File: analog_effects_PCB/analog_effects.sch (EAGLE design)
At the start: 24 parts, among them J1 575-4, J2 575-4, U1 TL082

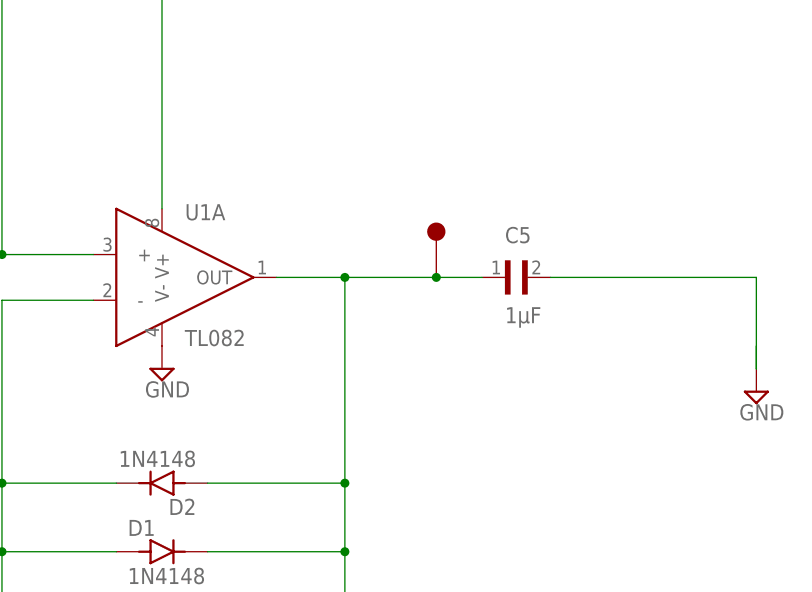
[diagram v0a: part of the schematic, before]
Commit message: added mux and digital pots to schematic
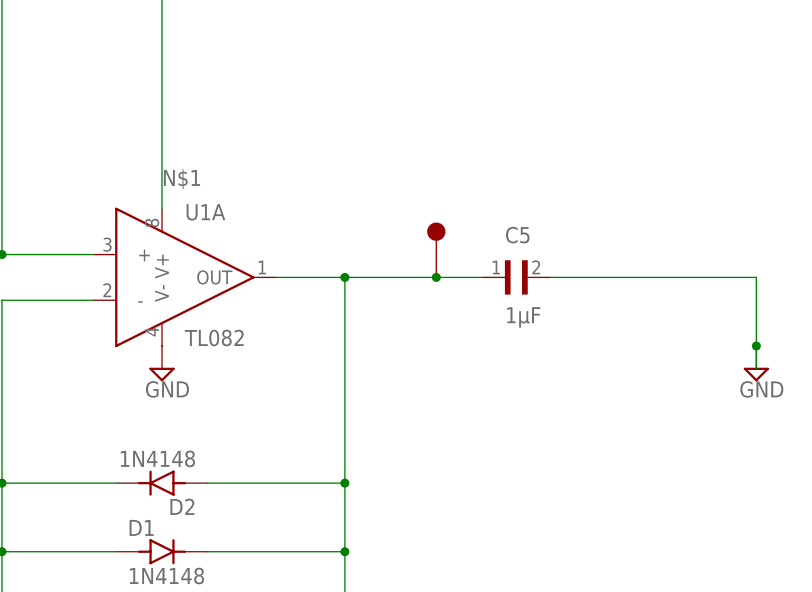
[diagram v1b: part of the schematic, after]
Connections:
- removed net N$10: C5.2
- net GND: now also C5.2
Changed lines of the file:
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@@
 <setting verticaltext="up"/>
 </settings>
-<grid distance="0.1" unitdist="inch" unit="inch" style="lines" multiple="1" display="no" altdistance="0.01" altunitdist="inch" altunit="inch"/>
+<grid distance="100" unitdist="mil" unit="mil" style="lines" multiple="1" display="no" altdistance="0.01" altunitdist="inch" altunit="inch"/>
 <layers>
 <layer number="1" name="Top" color="4" fill="1" visible="no" active="no"/>
@@
 <attribute name="VALUE" x="-17.78" y="116.8379" size="1.27105" layer="96"/>
 </instance>
-<instance part="SUPPLY4" gate="GND" x="182.88" y="99.06" smashed="yes">
-<attribute name="VALUE" x="180.975" y="95.885" size="1.778" layer="96"/>
+<instance part="SUPPLY4" gate="GND" x="182.88" y="101.6" smashed="yes">
+<attribute name="VALUE" x="180.975" y="98.425" size="1.778" layer="96"/>
 </instance>
 </instances>
@@
 <pinref part="R4" gate="G$1" pin="2"/>
 <wire x1="25.4" y1="180.34" x2="43.18" y2="180.34" width="0.1524" layer="91"/>
-<pinref part="U1" gate="A" pin="V+"/>
 <wire x1="43.18" y1="180.34" x2="106.68" y2="180.34" width="0.1524" layer="91"/>
-<wire x1="106.68" y1="180.34" x2="116.84" y2="180.34" width="0.1524" layer="91"/>
-<wire x1="116.84" y1="180.34" x2="116.84" y2="119.38" width="0.1524" layer="91"/>
 <junction x="43.18" y="180.34"/>
 <pinref part="TP5" gate="G$1" pin="TP"/>
-<junction x="106.68" y="180.34"/>
 <pinref part="BT1" gate="G$1" pin="+"/>
 <wire x1="0" y1="162.56" x2="0" y2="180.34" width="0.1524" layer="91"/>
 <wire x1="0" y1="180.34" x2="25.4" y2="180.34" width="0.1524" layer="91"/>
 <junction x="25.4" y="180.34"/>
+<pinref part="U1" gate="A" pin="V+"/>
+<wire x1="106.68" y1="180.34" x2="116.84" y2="180.34" width="0.1524" layer="91"/>
+<wire x1="116.84" y1="180.34" x2="116.84" y2="119.38" width="0.1524" layer="91"/>
+<junction x="106.68" y="180.34"/>
+<label x="116.84" y="121.92" size="1.778" layer="95"/>
 </segment>
 </net>
@@
 </segment>
 <segment>
+<pinref part="C5" gate="G$1" pin="2"/>
+<wire x1="160.02" y1="111.76" x2="182.88" y2="111.76" width="0.1524" layer="91"/>
+<wire x1="182.88" y1="111.76" x2="182.88" y2="104.14" width="0.1524" layer="91"/>
 <pinref part="SUPPLY4" gate="GND" pin="GND"/>
 <wire x1="182.88" y1="104.14" x2="182.88" y2="101.6" width="0.1524" layer="91"/>
+<junction x="182.88" y="104.14"/>
 </segment>
 </net>
@@
 <wire x1="91.44" y1="157.48" x2="93.98" y2="157.48" width="0.1524" layer="91"/>
 <pinref part="C3" gate="G$1" pin="2"/>
-<pinref part="U1" gate="A" pin="+"/>
 <wire x1="93.98" y1="157.48" x2="99.06" y2="157.48" width="0.1524" layer="91"/>
 <wire x1="71.12" y1="114.3" x2="83.82" y2="114.3" width="0.1524" layer="91"/>
 <wire x1="83.82" y1="114.3" x2="99.06" y2="114.3" width="0.1524" layer="91"/>
-<wire x1="99.06" y1="114.3" x2="109.22" y2="114.3" width="0.1524" layer="91"/>
 <wire x1="99.06" y1="157.48" x2="99.06" y2="114.3" width="0.1524" layer="91"/>
-<junction x="99.06" y="114.3"/>
 <pinref part="TP3" gate="G$1" pin="TP"/>
 <junction x="83.82" y="114.3"/>
 <pinref part="TP4" gate="G$1" pin="TP"/>
 <junction x="93.98" y="157.48"/>
+<pinref part="U1" gate="A" pin="+"/>
+<wire x1="99.06" y1="114.3" x2="109.22" y2="114.3" width="0.1524" layer="91"/>
+<junction x="99.06" y="114.3"/>
 </segment>
 </net>
@@
 </segment>
 </net>
-<net name="N$10" class="0">
-<segment>
-<pinref part="C5" gate="G$1" pin="2"/>
-<wire x1="160.02" y1="111.76" x2="182.88" y2="111.76" width="0.1524" layer="91"/>
-<wire x1="182.88" y1="111.76" x2="182.88" y2="101.6" width="0.1524" layer="91"/>
-</segment>
-</net>

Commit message: completed the digital pot circuitry on schematic
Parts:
- added J3: SAMTEC-SSQ-120-01-X-DJ, SAMTEC-SSQ-120-01-X-D:SAMTEC-SSQ-120-01-X-DJ
- added R10, R11, R12, R13, R14, R15, R7, R8, R9: 100kΩ, CRCW0603100KDHEAP:CRCW0603100KDHEAP
- added U2: AD5241BRZ1M, AD5241BRZ1M:AD5241BRZ1M
- added U3: AD5241BRZ10, AD5241BRZ10:AD5241BRZ10
- added U4: AD5241BRZ100, AD5241BRZ100:AD5241BRZ100
- added U5: TS5A3359DCUT, TS5A3359DCUT:TS5A3359DCUT
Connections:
- new net N$12: R10.1, U2.SHDN*
- new net N$13: R3.2, TP6.TP, U2.B1
- new net N$14: R11.2, U2.SDA
- new net N$15: R10.2, R11.1, R12.2, U2.VDD
- new net N$16: C5.2, U3.B1
- new net N$17: R12.1, U2.SCL
- new net N$19: R13.1, U4.SDA
- new net N$20: R13.2, R14.2, R15.2, U4.VDD
- new net N$21: R15.1, U4.SCL
- new net N$22: U3.W1, U4.B1
- new net N$23: R14.1, U4.~SHDN
- new net N$24: R7.1, U3.SDA
- new net N$25: R7.2, R8.2, R9.2, U3.VDD
- new net N$26: R9.1, U3.~SHDN
- new net N$27: R8.1, U3.SCL
- net GND: now also U2.AD0, U2.AD1, U2.DGND, U2.VSS, U3.AD0, U3.AD1, U3.DGND, U3.VSS, U4.AD0, U4.AD1, U4.DGND, U4.VSS, U4.W1; no longer C5.2
- net N$5: now also U2.W1; no longer R3.2, TP6.TP
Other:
- moved on the sheet: BT1, C1, C2, C3, C4, C5, C7, D1, D2, J1, J2, R1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

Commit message: Partly added Fuzz Circuit
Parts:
- added BT2: BC9VPC, BC9VPC:BC9VPC
- added C6: GRM188R6YA225KA12D, GRM188R6YA225KA12D:GRM188R6YA225KA12D
- added Q1, Q2: (no value), ngspice-simulation:BJT_PNP
- added R16: 100kΩ, CRCW0603100KDHEAP:CRCW0603100KDHEAP
- added R17: CRCW060333K0JNEAHP, CRCW060333K0JNEAHP:CRCW060333K0JNEAHP
- added R18: CRCW06038K20FKEAC, CRCW06038K20FKEAC:CRCW06038K20FKEAC
- added R19: CRCW0603470RJNEBC, CRCW0603470RJNEBC:CRCW0603470RJNEBC
- added U7: AD5258BRMZ1-R7, AD5258BRMZ1-R7:AD5258BRMZ1-R7
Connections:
- new net FUZZ_IN: C6.1
- new net N$10: Q1.E, Q2.B, R17.1
- new net N$11: BT2.-, R17.2, R19.2
- new net N$18: R18.1, R19.1
- new net N$28: Q2.C, R16.2
- new net N$9: C6.2, Q1.B, R16.1
- net GND: now also Q1.C
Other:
- moved on the sheet: BT1, C1, C2, C3, C4, C5, C7, D1, D2, J1, J2, J3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

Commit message: Added Mux logic to schematic. need to connect to Effects and decide if we have effect c or use as pass through
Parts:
- added C8: GCM188R91E104KA37J, GCM188R91E104KA37J:GCM188R91E104KA37J
- added C9: GRM188R61A226ME15D, GRM188R61A226ME15D:GRM188R61A226ME15D
- added U10, U11, U12, U13, U14, U8, U9: TS5A3359DCUT, TS5A3359DCUT:TS5A3359DCUT
- added U6: AD5258BRMZ1-R7, AD5258BRMZ1-R7:AD5258BRMZ1-R7
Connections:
- new net AUDIO_IN: U12.NO0, U13.NO0, U14.NO0
- new net A_OUT: U10.NO0, U11.NO0, U9.NO0
- new net B_OUT: U10.NO1, U11.NO1, U9.NO1
- new net C_OUT: U10.NO2, U11.NO2, U9.NO2
- new net MUX1_OUT: U10.COM, U12.NO1, U13.NO1, U14.NO1
- new net MUX1_S1: U10.IN1
- new net MUX1_S2: U10.IN2
- new net MUX2_OUT: U12.NO2, U13.NO2, U14.NO2, U9.COM
- new net MUX2_S1: U9.IN1
- new net MUX2_S2: U9.IN2
- new net MUX3_OUT: U11.COM
- new net MUX3_S1: U11.IN1
- new net MUX3_S2: U11.IN2
- new net MUX4_OUT: U12.COM
- new net MUX4_S1: U12.IN1
- new net MUX4_S2: U12.IN2
- new net MUX5_OUT: U13.COM
- new net MUX5_S1: U13.IN1
- new net MUX5_S2: U13.IN2
- new net MUX6_OUT: U14.COM
- new net MUX6_S1: U14.IN1
- new net MUX6_S2: U14.IN2
- new net N$29: C9.2, U7.W
- new net N$30: C8.2, U6.W
- new net N$31: U6.B
- new net N$38: U10.VCC
- new net N$39: U11.VCC
- new net N$40: U9.VCC
- new net N$41: U13.VCC
- new net N$42: U12.VCC
- new net N$56: U14.VCC
- net GND: now also C9.1, U10.GND, U11.GND, U12.GND, U13.GND, U14.GND, U6.A, U6.GND, U7.A, U7.GND, U9.GND
- net N$18: now also C8.1
- net N$28: now also U7.B

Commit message: Fixed Fuzz pot but need to change volume pot to 500k
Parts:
- removed U8: TS5A3359DCUT, TS5A3359DCUT:TS5A3359DCUT
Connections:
- removed net FUZZ_IN: C6.1
- new net 5V: J3.1, U7.VDD, U7.VLOGIC
- new net FUZZ_P1_SCL: U7.SCL
- new net FUZZ_P1_SDA: U7.SDA
- new net FUZZ_P2_SCL: U6.SCL
- new net FUZZ_P2_SDA: U6.SDA
- net MUX4_OUT: now also C6.1

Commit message: Schematic almost finalized missing aux in and out and possibly push buttons, starting layout
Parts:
- removed J1, J2: 575-4, 575-4:575-4
- removed R10: 100kΩ, CRCW0603100KDHEAP:CRCW0603100KDHEAP
- removed U3: AD5241BRZ10, AD5241BRZ10:AD5241BRZ10
- removed U5: TS5A3359DCUT, TS5A3359DCUT:TS5A3359DCUT
- removed U6: AD5258BRMZ1-R7, AD5258BRMZ1-R7:AD5258BRMZ1-R7
- added C10, C11, C12, C13, C14, C15, C16, C17, C18, C19, C20, C21: GCM188R91E104KA37J, GCM188R91E104KA37J:GCM188R91E104KA37J
- added TP10, TP11, TP12, TP13, TP14, TP15, TP16, TP17, TP18, TP19, TP20, TP7, TP8, TP9: 5015, 5015:5015
- added U8: AD5241BRZ1M, AD5241BRZ1M:AD5241BRZ1M
- R11, R12, R13, R14, R15, R7, R8, R9: value 100kΩ -> 10kΩ; device CRCW0603100KDHEAP:CRCW0603100KDHEAP -> MCT06030D1002BP100:MCT06030D1002BP100
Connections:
- removed net FUZZ_P1_SCL: U7.SCL
- removed net FUZZ_P1_SDA: U7.SDA
- removed net FUZZ_P2_SCL: U6.SCL
- removed net FUZZ_P2_SDA: U6.SDA
- removed net N$16: C5.2, U3.B1
- removed net N$24: R7.1, U3.SDA
- removed net N$25: R7.2, R8.2, R9.2, U3.VDD
- removed net N$26: R9.1, U3.~SHDN
- removed net N$27: R8.1, U3.SCL
- removed net N$31: U6.B
- removed net N$38: U10.VCC
- removed net N$39: U11.VCC
- removed net N$40: U9.VCC
- removed net N$41: U13.VCC
- removed net N$42: U12.VCC
- removed net N$56: U14.VCC
- new net POT_SCL: J3.5, R11.2, R12.2, R14.2, R7.2
- new net POT_SDA: J3.3, R13.1, R15.1, R8.1, R9.1
- net 5V: now also C10.2, C11.2, C12.2, C13.2, C14.2, C15.2, C16.2, C17.2, C18.2, C19.2, C20.2, C21.2, J3.2, TP19.TP, TP20.TP, U10.VCC, U11.VCC, U12.VCC, U13.VCC, U14.VCC, U2.SHDN*, U2.VDD, U4.AD1, U4.VDD, U4.~SHDN, U7.AD0, U7.AD1, U8.AD0, U8.SHDN*, U8.VDD, U9.VCC; no longer J3.1
- net A_OUT: now also TP12.TP, U8.B1
- net B_OUT: now also U4.W1
- net GND: now also C10.1, C11.1, C12.1, C13.1, C14.1, C15.1, C16.1, C17.1, C18.1, C19.1, C20.1, C21.1, J3.39, U8.AD1, U8.DGND, U8.VSS; no longer J2.1, U3.AD0, U3.AD1, U3.DGND, U3.VSS, U4.AD1, U4.W1, U6.A, U6.GND
- net MUX1_OUT: now also TP16.TP
- net MUX1_S1: now also J3.7
- net MUX1_S2: now also J3.29
- net MUX2_OUT: now also TP17.TP
- net MUX2_S1: now also J3.31
- net MUX2_S2: now also J3.26
- net MUX3_OUT: now also TP18.TP
- net MUX3_S1: now also J3.24
- net MUX3_S2: now also J3.21
- net MUX4_OUT: now also TP13.TP
- net MUX4_S1: now also J3.19
- net MUX4_S2: now also J3.23
- net MUX5_OUT: now also R1.1, TP14.TP
- net MUX5_S1: now also J3.32
- net MUX5_S2: now also J3.33
- net MUX6_OUT: now also TP15.TP
- net MUX6_S1: now also J3.8
- net MUX6_S2: now also J3.10
- net N$10: now also TP8.TP
- net N$11: now also TP9.TP
- net N$12: now also R8.2, U2.SDA; no longer R10.1, U2.SHDN*
- net N$14: now also R12.1, U8.SCL; no longer R11.2, U2.SDA
- net N$15: now also R9.2, U4.SDA; no longer R10.2, R11.1, R12.2, U2.VDD
- net N$17: now also R7.1; no longer R12.1
- net N$19: now also R13.2, U8.SDA; no longer R13.1, U4.SDA
- net N$20: now also R14.1, U7.SCL; no longer R13.2, R14.2, R15.2, U4.VDD
- net N$21: now also R11.1; no longer R15.1
- net N$22: now also C5.2; no longer U3.W1
- net N$23: now also R15.2, U7.SDA; no longer R14.1, U4.~SHDN
- net N$29: now also TP11.TP
- net N$30: now also TP10.TP, U8.A1; no longer U6.W
- net N$8: now also Q2.E, R18.2; no longer J1.1, R1.1
- net N$9: now also TP7.TP
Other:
- moved on the sheet: Q2, R11, R12, R13, R14, R15, R7, R8, R9, U2, U4

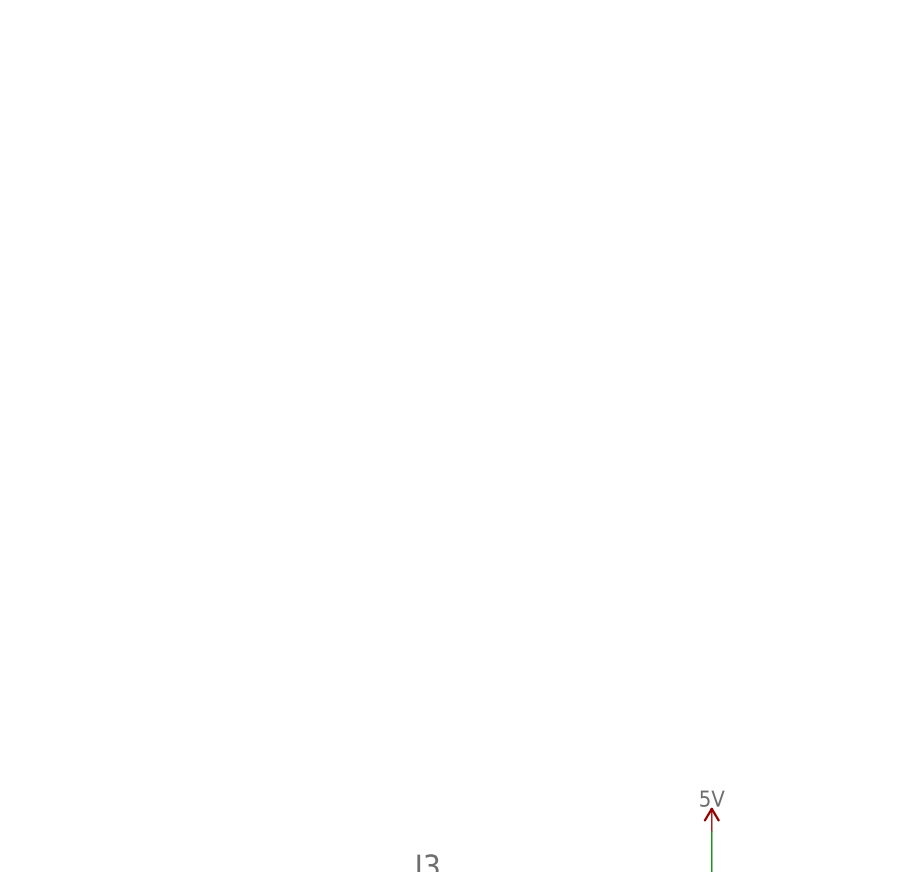
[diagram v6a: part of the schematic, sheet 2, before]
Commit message: Finalized schematic with connectos, next step layout
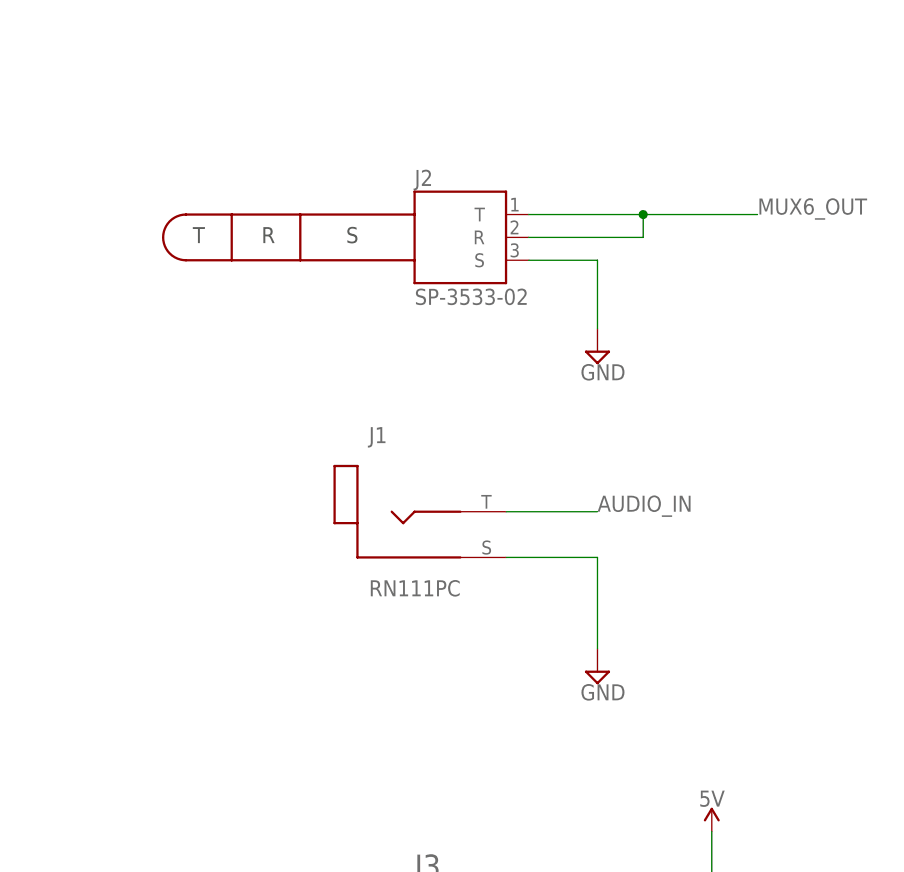
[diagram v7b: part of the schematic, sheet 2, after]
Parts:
- added J1: RN111PC, RN111PC:RN111PC
- added J2: SP-3533-02, SP-3533-02:SP-3533-02
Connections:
- net AUDIO_IN: now also J1.T
- net GND: now also J1.S, J2.S
- net MUX6_OUT: now also J2.R, J2.T
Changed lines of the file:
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@@
 <part name="SUPPLY43" library="SparkFun-PowerSymbols" library_urn="urn:adsk.eagle:library:530" deviceset="5V" device=""/>
 <part name="SUPPLY44" library="SparkFun-PowerSymbols" library_urn="urn:adsk.eagle:library:530" deviceset="5V" device=""/>
+<part name="J1" library="RN111PC" deviceset="RN111PC" device=""/>
+<part name="J2" library="SP-3533-02" deviceset="SP-3533-02" device=""/>
+<part name="SUPPLY4" library="supply2" library_urn="urn:adsk.eagle:library:372" deviceset="GND" device=""/>
+<part name="SUPPLY45" library="supply2" library_urn="urn:adsk.eagle:library:372" deviceset="GND" device=""/>
 </parts>
 <sheets>
@@
 <instance part="TP11" gate="G$1" x="172.72" y="238.76" smashed="yes" rot="R270"/>
 <instance part="TP12" gate="G$1" x="248.92" y="309.88" smashed="yes" rot="R270"/>
+<instance part="J1" gate="G$1" x="396.24" y="259.08" smashed="yes">
+<attribute name="NAME" x="391.16" y="266.7" size="1.778" layer="95"/>
+<attribute name="VALUE" x="391.16" y="251.46" size="1.778" layer="96" align="top-left"/>
+</instance>
+<instance part="J2" gate="G$1" x="406.4" y="289.56" smashed="yes">
+<attribute name="NAME" x="396.24" y="295.275" size="1.778" layer="95"/>
+<attribute name="VALUE" x="396.24" y="283.845" size="1.778" layer="96" align="top-left"/>
+</instance>
+<instance part="SUPPLY4" gate="GND" x="416.56" y="241.3" smashed="yes">
+<attribute name="VALUE" x="414.655" y="238.125" size="1.778" layer="96"/>
+</instance>
+<instance part="SUPPLY45" gate="GND" x="416.56" y="276.86" smashed="yes">
+<attribute name="VALUE" x="414.655" y="273.685" size="1.778" layer="96"/>
+</instance>
 </instances>
 <busses>
@@
 <wire x1="381" y1="165.1" x2="381" y2="149.86" width="0.1524" layer="91"/>
 </segment>
+<segment>
+<pinref part="J1" gate="G$1" pin="S"/>
+<wire x1="406.4" y1="254" x2="416.56" y2="254" width="0.1524" layer="91"/>
+<wire x1="416.56" y1="254" x2="416.56" y2="243.84" width="0.1524" layer="91"/>
+<pinref part="SUPPLY4" gate="GND" pin="GND"/>
+</segment>
+<segment>
+<pinref part="J2" gate="G$1" pin="S"/>
+<wire x1="408.94" y1="287.02" x2="416.56" y2="287.02" width="0.1524" layer="91"/>
+<wire x1="416.56" y1="287.02" x2="416.56" y2="279.4" width="0.1524" layer="91"/>
+<pinref part="SUPPLY45" gate="GND" pin="GND"/>
+</segment>
 </net>
 <net name="N$4" class="0">
@@
 </segment>
 </net>
+<net name="AUDIO_IN" class="0">
+<segment>
+<pinref part="J1" gate="G$1" pin="T"/>
+<wire x1="406.4" y1="259.08" x2="416.56" y2="259.08" width="0.1524" layer="91"/>
+<label x="416.56" y="259.08" size="1.778" layer="95"/>
+</segment>
+</net>
+<net name="MUX6_OUT" class="0">
+<segment>
+<pinref part="J2" gate="G$1" pin="R"/>
+<wire x1="408.94" y1="289.56" x2="421.64" y2="289.56" width="0.1524" layer="91"/>
+<wire x1="421.64" y1="289.56" x2="421.64" y2="292.1" width="0.1524" layer="91"/>
+<pinref part="J2" gate="G$1" pin="T"/>
+<wire x1="408.94" y1="292.1" x2="421.64" y2="292.1" width="0.1524" layer="91"/>
+<wire x1="421.64" y1="292.1" x2="434.34" y2="292.1" width="0.1524" layer="91"/>
+<junction x="421.64" y="292.1"/>
+<label x="434.34" y="292.1" size="1.778" layer="95"/>
+</segment>
+</net>

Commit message: Adding all files that were needed, Capstone is completed and it worked
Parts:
- removed BT1, BT2: BC9VPC, BC9VPC:BC9VPC
- removed J2: SP-3533-02, SP-3533-02:SP-3533-02
- added J4: SJ-3523-SMT-TR, SJ-3523-SMT-TR:SJ-3523-SMT-TR
- added R10, R20, R21, R22, R23, R24, R25, R26, R27, R28, R29, R30: MCT06030D1002BP100, MCT06030D1002BP100:MCT06030D1002BP100
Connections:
- removed net N$11: BT2.-, R17.2, R19.2, TP9.TP
- new net 9V_N: C4.2, C7.2, R17.2, R19.2, R5.1, TP2.TP, TP9.TP
- net 5V: now also R10.2, R20.2, R21.2, R22.2, R23.2, R24.2, R25.2, R26.2, R27.2, R28.2, R29.2, R30.2
- net GND: now also J4.1; no longer BT1.-, C4.2, C7.2, J2.S, R5.1, TP2.TP
- net MUX1_S1: now also R10.1
- net MUX1_S2: now also R20.1
- net MUX2_S1: now also R21.1
- net MUX2_S2: now also R22.1
- net MUX3_S1: now also R23.1
- net MUX3_S2: now also R24.1
- net MUX4_S1: now also R25.1
- net MUX4_S2: now also R26.1
- net MUX5_S1: now also R27.1
- net MUX5_S2: now also R28.1
- net MUX6_OUT: now also J4.2, J4.3; no longer J2.R, J2.T
- net MUX6_S1: now also R29.1
- net MUX6_S2: now also R30.1
- net N$1: no longer BT1.+
